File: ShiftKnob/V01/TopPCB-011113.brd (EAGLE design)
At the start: 33 x 33 mm, 8 parts

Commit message: final finalized versions of boards and fab files.
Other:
- board text added: "2-07-13"
- board text removed: "01-28-13"
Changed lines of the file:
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@@
 <circle x="17.78" y="17.78" radius="16.5" width="0.254" layer="20"/>
 <text x="27.051" y="20.2946" size="1.6764" layer="21" rot="R270">znelson1</text>
-<text x="29.3878" y="21.0312" size="1.6764" layer="21" rot="R270">01-28-13</text>
+<text x="29.3878" y="21.0312" size="1.6764" layer="21" rot="R270">2-07-13</text>
 <rectangle x1="29.2862" y1="23.5458" x2="29.8958" y2="23.5712" layer="21" rot="R90"/>
 <rectangle x1="28.8671" y1="23.5331" x2="30.2641" y2="23.5585" layer="21" rot="R90"/>
@@
 <text x="3.1496" y="17.145" size="0.8128" layer="21" font="vector" rot="R90">C1 </text>
 <text x="29.9212" y="21.082" size="1.778" layer="22" rot="MR270">znelson1</text>
-<text x="27.0002" y="21.1074" size="1.778" layer="22" rot="MR270">01-28-13</text>
+<text x="27.0002" y="21.1074" size="1.778" layer="22" rot="MR270">2-07-13</text>
 <rectangle x1="28.2448" y1="24.003" x2="28.8544" y2="24.0284" layer="22" rot="R90"/>
 <rectangle x1="27.8765" y1="23.9903" x2="29.2735" y2="24.0157" layer="22" rot="R90"/>
@@
 <contactref element="C1" pad="2"/>
 <contactref element="JP1" pad="2"/>
-<polygon width="0.6096" layer="1" isolate="0.4064">
+<polygon width="0.254" layer="1" isolate="0.4064">
 <vertex x="2.54" y="17.6022" curve="-90"/>
 <vertex x="17.7038" y="33.1978"/>

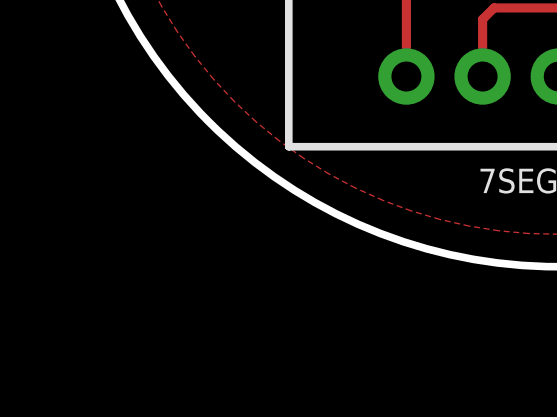
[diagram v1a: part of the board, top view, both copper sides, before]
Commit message: update schematics with new Ford frame.
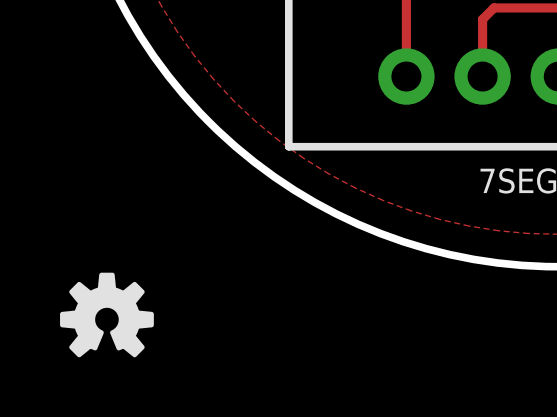
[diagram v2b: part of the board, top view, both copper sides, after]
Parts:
- added LOGO1: OSHW-LOGOS, SparkFun-Aesthetics:OSHW-LOGO-S
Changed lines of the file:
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@@
 <element name="U$2" library="SparkFun" package="OSHW-LOGO-S" value="OSHW-LOGOS" x="25.7048" y="22.86" rot="MR90"/>
 <element name="U$1" library="SparkFun" package="OSHW-LOGO-S" value="OSHW-LOGOS" x="31.5468" y="22.2758" rot="R90"/>
+<element name="LOGO1" library="SparkFun-Aesthetics" package="OSHW-LOGO-S" value="OSHW-LOGOS" x="2.7178" y="-0.4826"/>
 </elements>
 <signals>

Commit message: update with new frames and printed drawings for assembly.
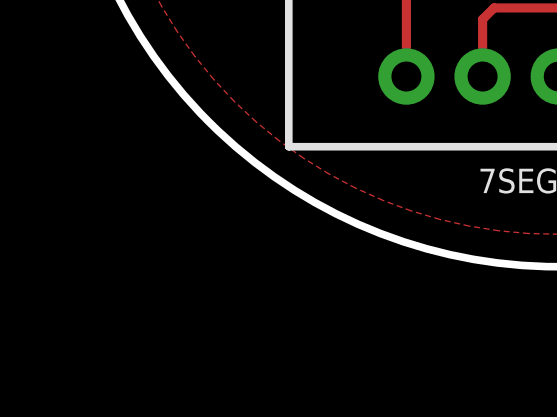
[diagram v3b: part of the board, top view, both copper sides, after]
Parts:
- removed LOGO1: OSHW-LOGOS, SparkFun-Aesthetics:OSHW-LOGO-S
- added U$3: (no value), FORD_frames:DOCFIELD
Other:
- board text added: "01"
- board text added: "Zachary Nelson znelson1@ford.com"
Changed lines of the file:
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@@
 <setting verticaltext="up"/>
 </settings>
-<grid distance="0.0254" unitdist="mm" unit="inch" style="lines" multiple="1" display="yes" altdistance="0.025" altunitdist="inch" altunit="inch"/>
+<grid distance="0.05" unitdist="inch" unit="inch" style="lines" multiple="1" display="yes" altdistance="0.025" altunitdist="inch" altunit="inch"/>
 <layers>
 <layer number="1" name="Top" color="4" fill="1" visible="yes" active="yes"/>
@@
 <layer number="150" name="Notes" color="7" fill="1" visible="yes" active="yes"/>
 <layer number="151" name="HeatSink" color="7" fill="1" visible="yes" active="yes"/>
+<layer number="175" name="transfer" color="13" fill="1" visible="yes" active="yes"/>
 <layer number="199" name="Contour" color="7" fill="1" visible="no" active="yes"/>
 <layer number="200" name="200bmp" color="1" fill="10" visible="yes" active="yes"/>
@@
 <rectangle x1="30.2133" y1="23.9903" x2="31.6611" y2="24.0157" layer="22" rot="R90"/>
 <rectangle x1="30.6451" y1="23.9903" x2="31.2801" y2="24.0157" layer="22" rot="R90"/>
-<dimension x1="17.844515625" y1="34.279875" x2="17.715484375" y2="1.280125" x3="43.7642" y3="17.6784" layer="48" dtype="diameter"/>
 <text x="15.0876" y="3.7338" size="0.8128" layer="21" font="vector">7SEGMENT</text>
+<text x="15.24" y="-40.64" size="3.81" layer="48">Zachary Nelson
+znelson1@ford.com</text>
+<text x="91.44" y="-39.37" size="3.81" layer="48">01</text>
+<wire x1="-49.53" y1="-17.78" x2="-49.53" y2="62.23" width="0.1016" layer="48"/>
+<wire x1="-49.53" y1="62.23" x2="102.87" y2="62.23" width="0.1016" layer="48"/>
+<wire x1="102.87" y1="62.23" x2="102.87" y2="-17.78" width="0.1016" layer="48"/>
+<dimension x1="17.78" y1="1.28" x2="17.78" y2="34.28" x3="-11.43" y3="17.78" layer="48" dtype="diameter"/>
 </plain>
 <attributes>
@@
 <element name="U$2" library="SparkFun" package="OSHW-LOGO-S" value="OSHW-LOGOS" x="25.7048" y="22.86" rot="MR90"/>
 <element name="U$1" library="SparkFun" package="OSHW-LOGO-S" value="OSHW-LOGOS" x="31.5468" y="22.2758" rot="R90"/>
-<element name="LOGO1" library="SparkFun-Aesthetics" package="OSHW-LOGO-S" value="OSHW-LOGOS" x="2.7178" y="-0.4826"/>
+<element name="U$3" library="FORD_frames" package="DOCFIELD" value="" x="-49.53" y="-48.26"/>
 </elements>
 <signals>
@@
 </board>
 </drawing>
+<compatibility>
+<note version="6.3" minversion="6.2.2" severity="warning">
+Since Version 6.2.2 text objects can contain more than one line,
+which will not be processed correctly with this version.
+</note>
+</compatibility>
 </eagle>
